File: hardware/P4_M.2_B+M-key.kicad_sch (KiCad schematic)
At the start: 87 parts, among them IC1 XT25F128FWOIGT-W, IC2 TPS563202DRLR, IC4 TPS563202DRLR, J2 USB_C_Receptacle_USB2.0_16P, Q2 MMDT2222A, U2 ESP32-P4NRW16, U3 EMMC04G-W627-M06U, U5 CH340K, Y1 32KHz, Y2 40MHz

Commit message: Updated module, now with uSD
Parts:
- removed C30: 4.7uF, Capacitor_SMD:C_0201_0603Metric, symbol P4_M.2_B+M-key-eagle-import:0201-CAPACITOR
- removed C31, C35, C36: 100nF, Capacitor_SMD:C_0201_0603Metric, symbol P4_M.2_B+M-key-eagle-import:0201-CAPACITOR
- removed R15, R16, R17: 51K, Resistor_SMD:R_0201_0603Metric, symbol P4_M.2_B+M-key-eagle-import:RESISTOR-0201-1/4W-1%
- removed R20: 10k, Resistor_SMD:R_0201_0603Metric, symbol P4_M.2_B+M-key-eagle-import:RESISTOR-0201-1/4W-1%
- removed R21: 100K, Resistor_SMD:R_0201_0603Metric, symbol P4_M.2_B+M-key-eagle-import:RESISTOR-0201-1/4W-1%
- removed U3: EMMC04G-W627-M06U, P4_M.2_B+M-key:BGA153N50P14X14_1300X1150X100N, symbol P4_M.2_B+M-key-eagle-import:EMMC04G-W627-M06U
- added C38: 100nF, Capacitor_SMD:C_0201_0603Metric, symbol P4_M.2_B+M-key-eagle-import:0201-CAPACITOR
- added J1: Micro_SD_Card_Det2, WHY:uSD_CARD, symbol Connector:Micro_SD_Card_Det2
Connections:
- net GND: now also C38.2, J1.11 (SHIELD), J1.6 (VSS)
- net SD_CMD: now also J1.3 (CMD)
- net SD_DATA0: now also J1.7 (DAT0)
- net SD_DATA1: now also J1.8 (DAT1)
- net SD_DATA2: now also J1.1 (DAT2)
- net SD_DATA3: now also J1.2 (DAT3/CD)
- net USB2HS_D+: now also U2.50 (DP), U4.3; no longer U2.49 (DM), U4.5
- net USB2HS_D-: now also U2.49 (DM), U4.5; no longer U2.50 (DP), U4.3
- net V/SDMMC: now also C38.1, J1.4 (VDD)
- net at R18.2: now also J1.5 (CLK)
- net SD_DATA4: no longer names the net of R14.2
- net SD_DATA4: now also J1.10 (DET_A); no longer U2.87 (GPIO45)
- net SD_DATA5 renamed SD_DET
- net SD_DET: now also J1.9 (DET_B)
- net SD_DATA6: no longer names the net of U2.89 (GPIO47)
- net SD_DATA7: no longer names the net of U2.90 (GPIO48)
- no-connect marks 30 -> 12
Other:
- note removed: "eMMC"
- moved on the sheet: R18

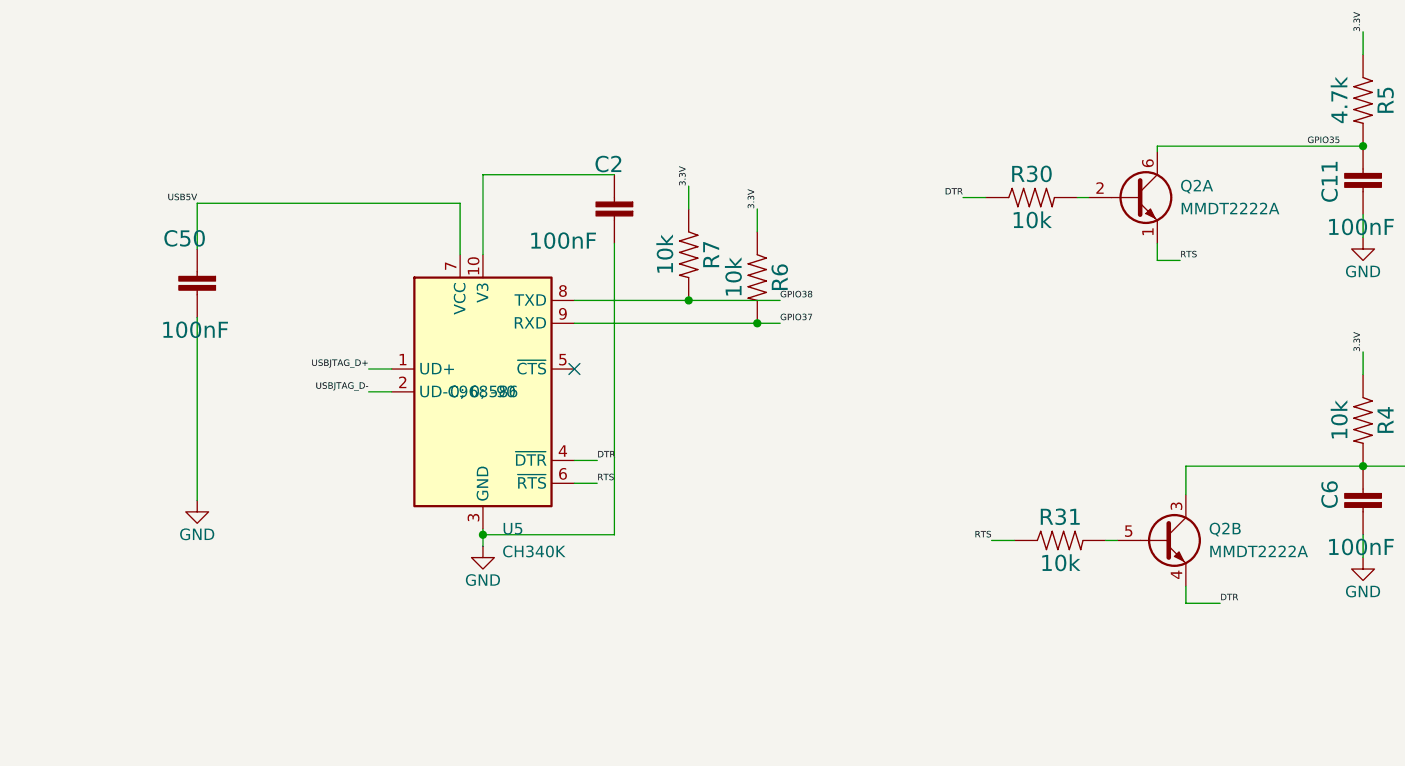
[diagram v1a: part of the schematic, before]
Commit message: Fixed mistakes from prototype 1
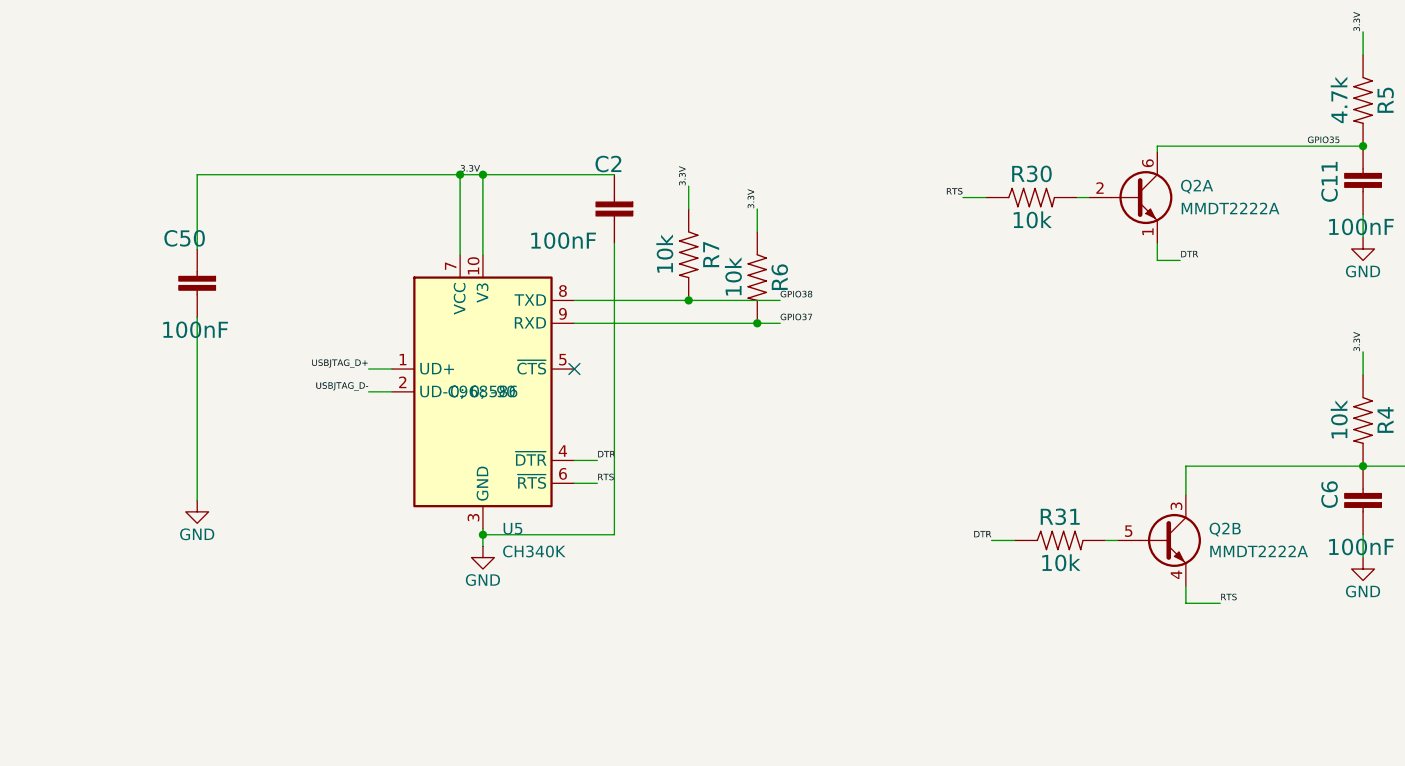
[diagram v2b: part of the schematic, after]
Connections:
- net 3.3V: now also C2.2, C50.2, U5.10 (V3), U5.7 (VCC)
- net DTR: now also Q2.1 (E1), R31.1; no longer Q2.4 (E2), R30.1
- net RTS: now also Q2.4 (E2), R30.1; no longer Q2.1 (E1), R31.1
- net USB5V: no longer C50.2, U5.7 (VCC)
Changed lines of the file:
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@@
 	)
 	(junction
+		(at 74.93 240.665)
+		(diameter 0)
+		(color 0 0 0 0)
+	)
+	(junction
 		(at 241.3 83.82)
 		(diameter 0)
@@
 	)
 	(junction
+		(at 77.47 240.665)
+		(diameter 0)
+		(color 0 0 0 0)
+	)
+	(junction
 		(at 231.14 154.94)
 		(diameter 0)
@@
 	(wire
 		(pts
-			(xy 74.93 243.84) (xy 74.93 249.555)
+			(xy 45.72 240.665) (xy 45.72 248.92)
 		)
 		(stroke
@@
 	(wire
 		(pts
-			(xy 45.72 243.84) (xy 45.72 248.92)
-		)
-		(stroke
-			(width 0.1524)
-			(type solid)
-		)
-	)
-	(wire
-		(pts
 			(xy 294.64 414.02) (xy 294.64 416.56)
 		)
@@
 	(wire
 		(pts
+			(xy 74.93 240.665) (xy 74.93 249.555)
+		)
+		(stroke
+			(width 0.1524)
+			(type solid)
+		)
+	)
+	(wire
+		(pts
 			(xy 99.06 355.6) (xy 99.06 342.9)
 		)
@@
 	(wire
 		(pts
+			(xy 74.93 240.665) (xy 77.47 240.665)
+		)
+		(stroke
+			(width 0)
+			(type default)
+		)
+	)
+	(wire
+		(pts
 			(xy 236.22 280.035) (xy 236.22 281.305)
 		)
@@
 	(wire
 		(pts
-			(xy 45.72 243.84) (xy 74.93 243.84)
+			(xy 45.72 240.665) (xy 74.93 240.665)
 		)
 		(stroke
@@
 		)
 	)
-	(label "USB5V"
-		(at 45.72 243.84 180)
-		(effects
-			(font
-				(size 0.7112 0.7112)
-			)
-			(justify right bottom)
-		)
-	)
 	(label "3.3V"
 		(at 269.24 137.16 0)
@@
 		)
 	)
+	(label "3.3V"
+		(at 74.93 240.665 0)
+		(effects
+			(font
+				(size 0.7112 0.7112)
+			)
+			(justify left bottom)
+		)
+	)
 	(label "I2S_LRCK"
 		(at 269.24 48.26 0)
@@
 	)
 	(label "DTR"
-		(at 130.81 243.205 180)
+		(at 154.94 250.19 0)
 		(effects
 			(font
 				(size 0.7112 0.7112)
 			)
-			(justify right bottom)
+			(justify left bottom)
 		)
 	)
@@
 	)
 	(label "RTS"
-		(at 154.94 250.19 0)
+		(at 130.81 243.205 180)
 		(effects
 			(font
 				(size 0.7112 0.7112)
 			)
-			(justify left bottom)
+			(justify right bottom)
 		)
 	)
@@
 	)
 	(label "DTR"
-		(at 159.385 288.29 0)
+		(at 133.985 281.305 180)
 		(effects
 			(font
 				(size 0.7112 0.7112)
 			)
-			(justify left bottom)
+			(justify right bottom)
 		)
 	)
@@
 	)
 	(label "RTS"
-		(at 133.985 281.305 180)
+		(at 159.385 288.29 0)
 		(effects
 			(font
 				(size 0.7112 0.7112)
 			)
-			(justify right bottom)
+			(justify left bottom)
 		)
 	)
